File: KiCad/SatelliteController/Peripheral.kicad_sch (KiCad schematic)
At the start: 3 parts, among them J2 CONN_RS485, U7 LTC485CN8#PBF

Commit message: 配線を避難させた
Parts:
- added J2: CONN_N2O_PRESS, TSRP_TerminalBlock_Alphaplus:TB401-1-4-E, symbol Connector_Generic:Conn_01x04
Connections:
- net GND: now also J2.1 (Pin_1)
- new net +12V: J2.4 (Pin_4)
- new net VREF_N2O_PRESS: J2.2 (Pin_2)
- no-connect marks 0 -> 1
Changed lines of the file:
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@@
   (junction (at 83.82 35.56) (diameter 0) (color 0 0 0 0)
   )
+  (no_connect (at 127 35.56))
   (wire (pts (xy 58.42 34.29) (xy 64.77 34.29))
     (stroke (width 0) (type default))
@@
     (stroke (width 0) (type default))
   )
+  (wire (pts (xy 132.08 40.64) (xy 127 40.64))
+    (stroke (width 0) (type default))
+  )
+  (wire (pts (xy 127 33.02) (xy 132.08 33.02))
+    (stroke (width 0) (type default))
+  )
   (wire (pts (xy 35.56 36.83) (xy 38.1 36.83))
     (stroke (width 0) (type default))
@@
     (stroke (width 0) (type default))
   )
+  (wire (pts (xy 127 38.1) (xy 134.62 38.1))
+    (stroke (width 0) (type default))
+  )
   (wire (pts (xy 67.31 26.67) (xy 67.31 29.21))
     (stroke (width 0) (type default))
@@
     (stroke (width 0) (type default))
   )
+  (wire (pts (xy 132.08 44.45) (xy 132.08 40.64))
+    (stroke (width 0) (type default))
+  )
   (wire (pts (xy 83.82 27.94) (xy 83.82 35.56))
     (stroke (width 0) (type default))
@@
     (stroke (width 0) (type default))
   )
+  (wire (pts (xy 132.08 33.02) (xy 132.08 29.21))
+    (stroke (width 0) (type default))
+  )
   (wire (pts (xy 33.02 36.83) (xy 35.56 36.83))
     (stroke (width 0) (type default))
   )
+  (rectangle (start 109.22 12.7) (end 161.29 60.96)
+    (stroke (width 0) (type default))
+    (fill (type none))
+  )
   (rectangle (start 12.7 12.7) (end 107.95 60.96)
     (stroke (width 0) (type default))
     (fill (type none))
+  )
+  (text "RS485" (at 110.49 15.24 0)
+    (effects (font (size 1.27 1.27)) (justify left bottom))
   )
   (text "RS485" (at 13.97 15.24 0)
@@
     )
   )
+  (global_label "VREF_N2O_PRESS" (shape output) (at 134.62 38.1 0) (fields_autoplaced)
+    (effects (font (size 1.27 1.27)) (justify left))
+    (property "Intersheetrefs" "${INTERSHEET_REFS}" (at 154.0357 38.1 0)
+      (effects (font (size 1.27 1.27)) (justify left) hide)
+    )
+  )
   (global_label "UART1_TX" (shape input) (at 35.56 41.91 180) (fields_autoplaced)
     (effects (font (size 1.27 1.27)) (justify right))
@@
         (path "/628d040b-43bf-4733-804f-091644a90124/092bb5f6-479a-4342-8285-14bd550a4a8c"
           (reference "R26") (unit 1)
+        )
+      )
+    )
+  )
+  (symbol (lib_id "power:+12V") (at 132.08 29.21 0) (unit 1)
+    (in_bom yes) (on_board yes) (dnp no) (fields_autoplaced)
+    (property "Reference" "#PWR040" (at 132.08 33.02 0)
+      (effects (font (size 1.27 1.27)) hide)
+    )
+    (property "Value" "+12V" (at 132.08 25.4 0)
+      (effects (font (size 1.27 1.27)))
+    )
+    (property "Footprint" "" (at 132.08 29.21 0)
+      (effects (font (size 1.27 1.27)) hide)
+    )
+    (property "Datasheet" "" (at 132.08 29.21 0)
+      (effects (font (size 1.27 1.27)) hide)
+    )
+    (pin "1")
+    (instances
+      (project "SatelliteController"
+        (path "/628d040b-43bf-4733-804f-091644a90124/092bb5f6-479a-4342-8285-14bd550a4a8c"
+          (reference "#PWR040") (unit 1)
         )
       )
@@
         )
       )
+    )
+  )
+  (symbol (lib_id "power:GND") (at 132.08 44.45 0) (unit 1)
+    (in_bom yes) (on_board yes) (dnp no) (fields_autoplaced)
+    (property "Reference" "#PWR039" (at 132.08 50.8 0)
+      (effects (font (size 1.27 1.27)) hide)
+    )
+    (property "Value" "GND" (at 132.08 49.53 0)
+      (effects (font (size 1.27 1.27)))
+    )
+    (property "Footprint" "" (at 132.08 44.45 0)
+      (effects (font (size 1.27 1.27)) hide)
+    )
+    (property "Datasheet" "" (at 132.08 44.45 0)
+      (effects (font (size 1.27 1.27)) hide)
+    )
+    (pin "1")
+    (instances
+      (project "SatelliteController"
+        (path "/628d040b-43bf-4733-804f-091644a90124/092bb5f6-479a-4342-8285-14bd550a4a8c"
+          (reference "#PWR039") (unit 1)
+        )
+      )
+    )
+  )
+  (symbol (lib_id "Connector_Generic:Conn_01x04") (at 121.92 38.1 180) (unit 1)
+    (in_bom yes) (on_board yes) (dnp no) (fields_autoplaced)
+    (property "Reference" "J2" (at 121.92 27.94 0)
+      (effects (font (size 1.27 1.27)))
+    )
+    (property "Value" "CONN_N2O_PRESS" (at 121.92 30.48 0)
+      (effects (font (size 1.27 1.27)))
+    )
+    (property "Footprint" "TSRP_TerminalBlock_Alphaplus:TB401-1-4-E" (at 121.92 38.1 0)
+      (effects (font (size 1.27 1.27)) hide)
+    )
+    (property "Datasheet" "https://akizukidenshi.com/catalog/g/gP-07756/" (at 121.92 38.1 0)
+      (effects (font (size 1.27 1.27)) hide)
+    )
+    (property "LCSC" "" (at 121.92 38.1 0)
+      (effects (font (size 1.27 1.27)) hide)
+    )
+    (pin "1")
+    (pin "2")
+    (pin "3")
+    (pin "4")
+    (instances
+      (project "SatelliteController"
+        (path "/628d040b-43bf-4733-804f-091644a90124"
+          (reference "J2") (unit 1)
+        )
+        (path "/628d040b-43bf-4733-804f-091644a90124/092bb5f6-479a-4342-8285-14bd550a4a8c"
+          (reference "J9") (unit 1)
+        )
+      )

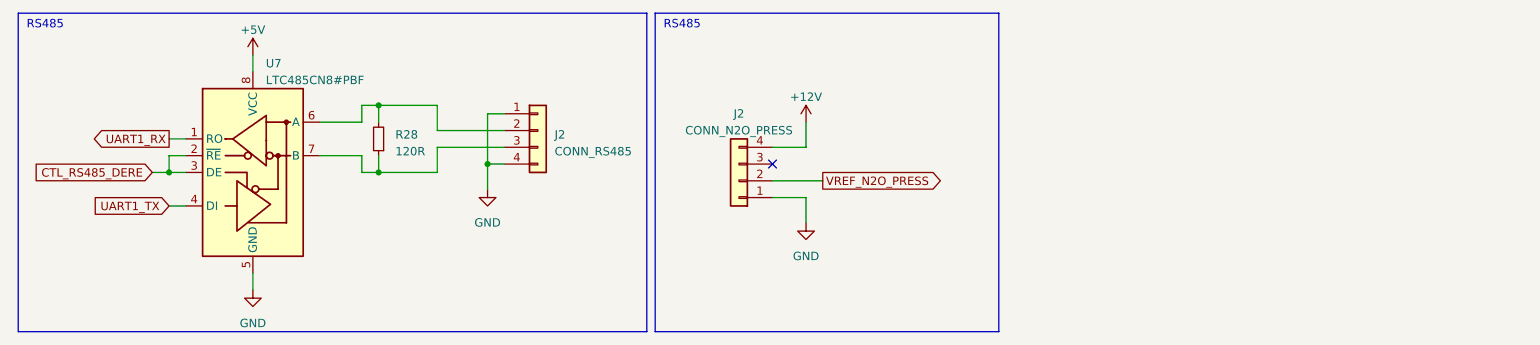
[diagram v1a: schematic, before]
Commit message: サテコンのボード図を作成
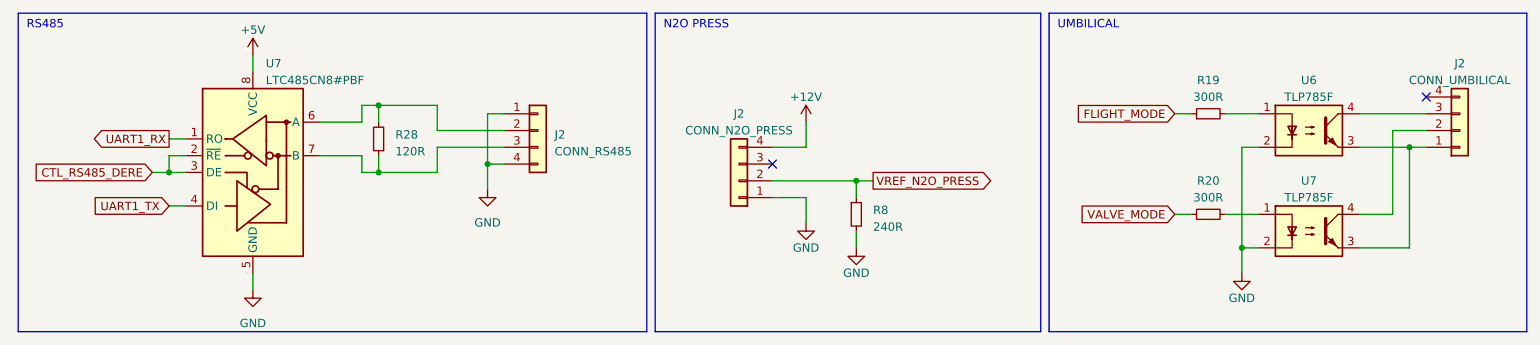
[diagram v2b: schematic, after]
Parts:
- added J2: CONN_UMBILICAL, TSRP_TerminalBlock_Alphaplus:TB401-1-4-E, symbol Connector_Generic:Conn_01x04
- added R19, R20: 300R, Resistor_SMD:R_0603_1608Metric_Pad0.98x0.95mm_HandSolder, symbol Device:R_Small
- added R8: 240R, Resistor_SMD:R_0603_1608Metric_Pad0.98x0.95mm_HandSolder, symbol Device:R_Small
- added U6, U7: TLP785F, Package_DIP:DIP-4_W10.16mm, symbol Isolator:TLP785F
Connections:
- net GND: now also R8.2, U6.2, U7.2
- net VREF_N2O_PRESS: now also R8.1
- new net: R20.2, U7.1
- new net: R19.2, U6.1
- new net: J2.1 (Pin_1), U6.3, U7.3
- new net: J2.2 (Pin_2), U7.4
- new net: J2.3 (Pin_3), U6.4
- new net FLIGHT_MODE: R19.1
- new net VALVE_MODE: R20.1
- no-connect marks 1 -> 2
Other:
- note added: "N2O PRESS"
- note added: "UMBILICAL"

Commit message: GSEのパーツリストを作成
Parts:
- R8: value 240R -> 270R
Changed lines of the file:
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@@
       (effects (font (size 1.27 1.27)) (justify left))
     )
-    (property "Value" "240R" (at 142.24 45.085 0)
+    (property "Value" "270R" (at 142.24 45.085 0)
       (effects (font (size 1.27 1.27)) (justify left))
     )

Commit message: サテコンのクリスマスツリーを削除
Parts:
- renumbered J2 to J10, J2 to J15, J2 to J9, R28 to R26, U7 to U8

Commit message: 電磁弁制御回路を整理
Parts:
- R24: renamed from R8; value 270R -> 240R
- renumbered J9 to J10, J10 to J11, J15 to J9, R26 to R23, R19 to R25, R20 to R26, U8 to U6, U6 to U7, U7 to U8
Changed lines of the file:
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@@
 		(dnp no)
 		(fields_autoplaced yes)
-		(property "Reference" "R20"
+		(property "Reference" "R26"
 			(at 193.04 38.1 90)
 			(effects
@@
 			(project "SatelliteController"
 				(path "/628d040b-43bf-4733-804f-091644a90124/092bb5f6-479a-4342-8285-14bd550a4a8c"
-					(reference "R20")
+					(reference "R26")
 					(unit 1)
 				)
@@
 		(dnp no)
 		(fields_autoplaced yes)
-		(property "Reference" "#PWR059"
+		(property "Reference" "#PWR052"
 			(at 83.82 45.72 0)
 			(effects
@@
 			(project "SatelliteController"
 				(path "/628d040b-43bf-4733-804f-091644a90124/092bb5f6-479a-4342-8285-14bd550a4a8c"
-					(reference "#PWR059")
+					(reference "#PWR052")
 					(unit 1)
 				)
@@
 		(dnp no)
 		(fields_autoplaced yes)
-		(property "Reference" "R8"
+		(property "Reference" "R24"
 			(at 142.24 42.545 0)
 			(effects
@@
 			)
 		)
-		(property "Value" "270R"
+		(property "Value" "240R"
 			(at 142.24 45.085 0)
 			(effects
@@
 			(project "SatelliteController"
 				(path "/628d040b-43bf-4733-804f-091644a90124/092bb5f6-479a-4342-8285-14bd550a4a8c"
-					(reference "R8")
+					(reference "R24")
 					(unit 1)
 				)
@@
 		(on_board yes)
 		(dnp no)
-		(property "Reference" "#PWR044"
+		(property "Reference" "#PWR055"
 			(at 139.7 54.61 0)
 			(effects
@@
 			(project "SatelliteController"
 				(path "/628d040b-43bf-4733-804f-091644a90124/092bb5f6-479a-4342-8285-14bd550a4a8c"
-					(reference "#PWR044")
+					(reference "#PWR055")
 					(unit 1)
 				)
@@
 		(on_board yes)
 		(dnp no)
-		(property "Reference" "#PWR039"
+		(property "Reference" "#PWR054"
 			(at 132.08 50.8 0)
 			(effects
@@
 			(project "SatelliteController"
 				(path "/628d040b-43bf-4733-804f-091644a90124/092bb5f6-479a-4342-8285-14bd550a4a8c"
-					(reference "#PWR039")
+					(reference "#PWR054")
 					(unit 1)
 				)
@@
 		(dnp no)
 		(fields_autoplaced yes)
-		(property "Reference" "R19"
+		(property "Reference" "R25"
 			(at 193.04 22.86 90)
 			(effects
@@
 			(project "SatelliteController"
 				(path "/628d040b-43bf-4733-804f-091644a90124/092bb5f6-479a-4342-8285-14bd550a4a8c"
-					(reference "R19")
+					(reference "R25")
 					(unit 1)
 				)
@@
 		(dnp no)
 		(fields_autoplaced yes)
-		(property "Reference" "#PWR056"
+		(property "Reference" "#PWR050"
 			(at 48.26 22.86 0)
 			(effects
@@
 			(project "SatelliteController"
 				(path "/628d040b-43bf-4733-804f-091644a90124/092bb5f6-479a-4342-8285-14bd550a4a8c"
-					(reference "#PWR056")
+					(reference "#PWR050")
 					(unit 1)
 				)
@@
 		(dnp no)
 		(fields_autoplaced yes)
-		(property "Reference" "U7"
+		(property "Reference" "U8"
 			(at 208.28 38.1 0)
 			(effects
@@
 			(project "SatelliteController"
 				(path "/628d040b-43bf-4733-804f-091644a90124/092bb5f6-479a-4342-8285-14bd550a4a8c"
-					(reference "U7")
+					(reference "U8")
 					(unit 1)
 				)
@@
 		(dnp no)
 		(fields_autoplaced yes)
-		(property "Reference" "R26"
+		(property "Reference" "R23"
 			(at 69.85 31.115 0)
 			(effects
@@
 			(project "SatelliteController"
 				(path "/628d040b-43bf-4733-804f-091644a90124/092bb5f6-479a-4342-8285-14bd550a4a8c"
-					(reference "R26")
+					(reference "R23")
 					(unit 1)
 				)
@@
 		(dnp no)
 		(fields_autoplaced yes)
-		(property "Reference" "#PWR040"
+		(property "Reference" "#PWR053"
 			(at 132.08 33.02 0)
 			(effects
@@
 			(project "SatelliteController"
 				(path "/628d040b-43bf-4733-804f-091644a90124/092bb5f6-479a-4342-8285-14bd550a4a8c"
-					(reference "#PWR040")
+					(reference "#PWR053")
 					(unit 1)
 				)
@@
 		(dnp no)
 		(fields_autoplaced yes)
-		(property "Reference" "J15"
+		(property "Reference" "J9"
 			(at 93.98 31.115 0)
 			(effects
@@
 			(project "SatelliteController"
 				(path "/628d040b-43bf-4733-804f-091644a90124/092bb5f6-479a-4342-8285-14bd550a4a8c"
-					(reference "J15")
+					(reference "J9")
 					(unit 1)
 				)
@@
 		(dnp no)
 		(fields_autoplaced yes)
-		(property "Reference" "U6"
+		(property "Reference" "U7"
 			(at 208.28 22.86 0)
 			(effects
@@
 			(project "SatelliteController"
 				(path "/628d040b-43bf-4733-804f-091644a90124/092bb5f6-479a-4342-8285-14bd550a4a8c"
-					(reference "U6")
+					(reference "U7")
 					(unit 1)
 				)
@@
 		(dnp no)
 		(fields_autoplaced yes)
-		(property "Reference" "U8"
+		(property "Reference" "U6"
 			(at 50.2159 20.32 0)
 			(effects
@@
 			(project "SatelliteController"
 				(path "/628d040b-43bf-4733-804f-091644a90124/092bb5f6-479a-4342-8285-14bd550a4a8c"
-					(reference "U8")
+					(reference "U6")
 					(unit 1)
 				)
@@
 		(on_board yes)
 		(dnp no)
-		(property "Reference" "#PWR049"
+		(property "Reference" "#PWR056"
 			(at 198.12 58.42 0)
 			(effects
@@
 			(project "SatelliteController"
 				(path "/628d040b-43bf-4733-804f-091644a90124/092bb5f6-479a-4342-8285-14bd550a4a8c"
-					(reference "#PWR049")
+					(reference "#PWR056")
 					(unit 1)
 				)
@@
 		(dnp no)
 		(fields_autoplaced yes)
-		(property "Reference" "#PWR061"
+		(property "Reference" "#PWR051"
 			(at 48.26 60.96 0)
 			(effects
@@
 			(project "SatelliteController"
 				(path "/628d040b-43bf-4733-804f-091644a90124/092bb5f6-479a-4342-8285-14bd550a4a8c"
-					(reference "#PWR061")
+					(reference "#PWR051")
 					(unit 1)
 				)
@@
 		(dnp no)
 		(fields_autoplaced yes)
-		(property "Reference" "J10"
+		(property "Reference" "J11"
 			(at 231.14 20.32 0)
 			(effects
@@
 			(project "SatelliteController"
 				(path "/628d040b-43bf-4733-804f-091644a90124/092bb5f6-479a-4342-8285-14bd550a4a8c"
-					(reference "J10")
+					(reference "J11")
 					(unit 1)
 				)
@@
 		(dnp no)
 		(fields_autoplaced yes)
-		(property "Reference" "J9"
+		(property "Reference" "J10"
 			(at 121.92 27.94 0)
 			(effects
@@
 			(project "SatelliteController"
 				(path "/628d040b-43bf-4733-804f-091644a90124/092bb5f6-479a-4342-8285-14bd550a4a8c"
-					(reference "J9")
-					(unit 1)
-				)
+					(reference "J10")
+					(unit 1)
+				)

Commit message: 配線
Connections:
- net GND: now also J10.3 (Pin_3)
- no-connect marks 2 -> 1
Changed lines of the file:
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@@
+	)
+	(junction
+		(at 132.08 40.64)
+		(diameter 0)
+		(color 0 0 0 0)
 	)
 	(junction
@@
 		(at 226.06 25.4)
 	)
-	(no_connect
-		(at 127 35.56)
-	)
 	(wire
 		(pts
@@
 	(wire
 		(pts
+			(xy 127 35.56) (xy 132.08 35.56)
+		)
+		(stroke
+			(width 0)
+			(type default)
+		)
+	)
+	(wire
+		(pts
 			(xy 187.96 43.18) (xy 190.5 43.18)
 		)
@@
 		)
 		(stroke
+			(width 0)
+			(type default)
+		)
+	)
+	(wire
+		(pts
+			(xy 132.08 35.56) (xy 132.08 40.64)
+		)
+		(stroke

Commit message: シルクを修正
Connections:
- net at J11.1 (Pin_1), U8.3: no longer U7.3
- net at J11.4 (Pin_4): now also U7.3
- no-connect marks 1 -> 0
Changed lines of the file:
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@@
-	)
-	(junction
-		(at 223.52 33.02)
-		(diameter 0)
-		(color 0 0 0 0)
 	)
 	(junction
@@
 		(color 0 0 0 0)
 	)
-	(no_connect
-		(at 226.06 25.4)
-	)
 	(wire
 		(pts
@@
 	(wire
 		(pts
+			(xy 215.9 33.02) (xy 218.44 33.02)
+		)
+		(stroke
+			(width 0)
+			(type default)
+		)
+	)
+	(wire
+		(pts
 			(xy 58.42 29.21) (xy 64.77 29.21)
 		)
@@
 	(wire
 		(pts
+			(xy 218.44 33.02) (xy 218.44 25.4)
+		)
+		(stroke
+			(width 0)
+			(type default)
+		)
+	)
+	(wire
+		(pts
 			(xy 220.98 43.18) (xy 215.9 43.18)
 		)
@@
 	(wire
 		(pts
+			(xy 218.44 25.4) (xy 226.06 25.4)
+		)
+		(stroke
+			(width 0)
+			(type default)
+		)
+	)
+	(wire
+		(pts
 			(xy 187.96 43.18) (xy 190.5 43.18)
 		)
@@
 		)
 		(stroke
-			(width 0)
-			(type default)
-		)
-	)
-	(wire
-		(pts
-			(xy 215.9 33.02) (xy 223.52 33.02)
-		)
-		(stroke
